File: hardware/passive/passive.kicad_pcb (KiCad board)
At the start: 2 copper layers, 45 x 17 mm, 8 parts, among them J1 i/O, J2 Conn 1, J3 Conn 2

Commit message: Passive board updates
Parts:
- H1, H2, H3, H4: footprint cycfi_library:mounting_hole_2.1mm -> cycfi_library:mounting_hole_st1.9; moved to F.Cu
- moved J3 0.50 mm to (143.3, 108.5)
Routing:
- net out-: track 21.7 -> 24.2 mm
- net int_coil+: track 18.3 -> 20.3 mm
- removed copper zone on B.Cu, net int_coil+
- removed copper zone on B.Cu, net out-
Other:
- board text added: "XR Spectra Passive v1.01"
- board text removed: "XR Spectra Passive v1.0"
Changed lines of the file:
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@@
     (thickness 1.6)
     (drawings 24)
-    (tracks 42)
+    (tracks 47)
     (zones 0)
     (modules 8)
@@
     (44 Edge.Cuts user)
     (45 Margin user)
-    (46 B.CrtYd user hide)
-    (47 F.CrtYd user hide)
-    (48 B.Fab user hide)
-    (49 F.Fab user hide)
+    (46 B.CrtYd user)
+    (47 F.CrtYd user)
+    (48 B.Fab user)
+    (49 F.Fab user)
   )
   (setup
@@
     (add_net out-)
   )
+  (module cycfi_library:mounting_hole_st1.9 (layer F.Cu)
+    (at 148 115)
+    (descr "Mounting Hole 2.1mm, no annular")
+    (tags "mounting hole 2.1mm no annular")
+    (attr virtual)
+    (fp_text reference H4 (at 0 -3.2) (layer F.SilkS) hide
+      (effects (font (size 1 1) (thickness 0.15)))
+    )
+    (fp_text value MountingHole (at 0 3.2) (layer F.Fab) hide
+      (effects (font (size 1 1) (thickness 0.15)))
+    )
+    (fp_text user %R (at 0.3 0) (layer F.Fab)
+      (effects (font (size 1 1) (thickness 0.15)))
+    )
+    (fp_circle (center 0 0) (end 1.75 0) (layer F.CrtYd) (width 0.05))
+    (pad "" np_thru_hole circle (at 0 0) (size 2 2) (drill 2) (layers *.Cu *.Mask))
+  )
+  (module cycfi_library:mounting_hole_st1.9 (layer F.Cu)
+    (at 148 102)
+    (descr "Mounting Hole 2.1mm, no annular")
+    (tags "mounting hole 2.1mm no annular")
+    (attr virtual)
+    (fp_text reference H3 (at 0 -3.2 180) (layer F.SilkS) hide
+      (effects (font (size 1 1) (thickness 0.15)))
+    )
+    (fp_text value MountingHole (at 0 3.2 180) (layer F.Fab) hide
+      (effects (font (size 1 1) (thickness 0.15)))
+    )
+    (fp_text user %R (at 0.3 0 180) (layer F.Fab)
+      (effects (font (size 1 1) (thickness 0.15)))
+    )
+    (fp_circle (center 0 0) (end 1.75 0) (layer F.CrtYd) (width 0.05))
+    (pad "" np_thru_hole circle (at 0 0) (size 2 2) (drill 2) (layers *.Cu *.Mask))
+  )
+  (module cycfi_library:mounting_hole_st1.9 (layer F.Cu)
+    (at 107 115)
+    (descr "Mounting Hole 2.1mm, no annular")
+    (tags "mounting hole 2.1mm no annular")
+    (attr virtual)
+    (fp_text reference H2 (at 0 -3.2) (layer F.SilkS) hide
+      (effects (font (size 1 1) (thickness 0.15)))
+    )
+    (fp_text value MountingHole (at 0 3.2) (layer F.Fab) hide
+      (effects (font (size 1 1) (thickness 0.15)))
+    )
+    (fp_text user %R (at 0.3 0) (layer F.Fab)
+      (effects (font (size 1 1) (thickness 0.15)))
+    )
+    (fp_circle (center 0 0) (end 1.75 0) (layer F.CrtYd) (width 0.05))
+    (pad "" np_thru_hole circle (at 0 0) (size 2 2) (drill 2) (layers *.Cu *.Mask))
+  )
+  (module cycfi_library:mounting_hole_st1.9 (layer F.Cu)
+    (at 107 102)
+    (descr "Mounting Hole 2.1mm, no annular")
+    (tags "mounting hole 2.1mm no annular")
+    (attr virtual)
+    (fp_text reference H1 (at 0 -3.2) (layer F.SilkS) hide
+      (effects (font (size 1 1) (thickness 0.15)))
+    )
+    (fp_text value MountingHole (at 0 3.2) (layer F.Fab) hide
+      (effects (font (size 1 1) (thickness 0.15)))
+    )
+    (fp_text user %R (at 0.3 0) (layer F.Fab)
+      (effects (font (size 1 1) (thickness 0.15)))
+    )
+    (fp_circle (center 0 0) (end 1.75 0) (layer F.CrtYd) (width 0.05))
+    (pad "" np_thru_hole circle (at 0 0) (size 2 2) (drill 2) (layers *.Cu *.Mask))
+  )
   (module cycfi_library:pin_socket_2x3p_1.00mm_smd_vertical (layer B.Cu)
     (at 146.5 108.5 90)
@@
   )
   (module cycfi_library:pin_socket_2x3p_1.00mm_smd_vertical (layer B.Cu)
-    (at 142.8 108.5 90)
+    (at 143.3 108.5 90)
     (descr "surface-mounted straight pin header, 2x03, 1.00mm pitch, double rows")
     (tags "Surface mounted pin header SMD 2x03 1.00mm double row")
@@
       (rotate (xyz 0 0 0))
     )
-  )
-  (module cycfi_library:mounting_hole_2.1mm (layer B.Cu)
-    (at 148 115)
-    (descr "Mounting Hole 2.1mm, no annular")
-    (tags "mounting hole 2.1mm no annular")
-    (attr virtual)
-    (fp_text reference H4 (at 0 3.2) (layer B.SilkS) hide
-      (effects (font (size 1 1) (thickness 0.15)) (justify mirror))
-    )
-    (fp_text value MountingHole (at 0 -3.2) (layer B.Fab)
-      (effects (font (size 1 1) (thickness 0.15)) (justify mirror))
-    )
-    (fp_text user %R (at 0.3 0) (layer B.Fab)
-      (effects (font (size 1 1) (thickness 0.15)) (justify mirror))
-    )
-    (fp_circle (center 0 0) (end 2.35 0) (layer B.CrtYd) (width 0.05))
-    (pad "" np_thru_hole circle (at 0 0) (size 2.1 2.1) (drill 2.1) (layers *.Cu *.Mask))
-  )
-  (module cycfi_library:mounting_hole_2.1mm (layer B.Cu)
-    (at 148 102)
-    (descr "Mounting Hole 2.1mm, no annular")
-    (tags "mounting hole 2.1mm no annular")
-    (attr virtual)
-    (fp_text reference H3 (at 0 3.2) (layer B.SilkS) hide
-      (effects (font (size 1 1) (thickness 0.15)) (justify mirror))
-    )
-    (fp_text value MountingHole (at 0 -3.2) (layer B.Fab)
-      (effects (font (size 1 1) (thickness 0.15)) (justify mirror))
-    )
-    (fp_text user %R (at 0.3 0) (layer B.Fab)
-      (effects (font (size 1 1) (thickness 0.15)) (justify mirror))
-    )
-    (fp_circle (center 0 0) (end 2.35 0) (layer B.CrtYd) (width 0.05))
-    (pad "" np_thru_hole circle (at 0 0) (size 2.1 2.1) (drill 2.1) (layers *.Cu *.Mask))
-  )
-  (module cycfi_library:mounting_hole_2.1mm (layer B.Cu)
-    (at 107 115)
-    (descr "Mounting Hole 2.1mm, no annular")
-    (tags "mounting hole 2.1mm no annular")
-    (attr virtual)
-    (fp_text reference H2 (at 0 3.2) (layer B.SilkS) hide
-      (effects (font (size 1 1) (thickness 0.15)) (justify mirror))
-    )
-    (fp_text value MountingHole (at 0 -3.2) (layer B.Fab)
-      (effects (font (size 1 1) (thickness 0.15)) (justify mirror))
-    )
-    (fp_text user %R (at 0.3 0) (layer B.Fab)
-      (effects (font (size 1 1) (thickness 0.15)) (justify mirror))
-    )
-    (fp_circle (center 0 0) (end 2.35 0) (layer B.CrtYd) (width 0.05))
-    (pad "" np_thru_hole circle (at 0 0) (size 2.1 2.1) (drill 2.1) (layers *.Cu *.Mask))
-  )
-  (module cycfi_library:mounting_hole_2.1mm (layer B.Cu)
-    (at 107 102)
-    (descr "Mounting Hole 2.1mm, no annular")
-    (tags "mounting hole 2.1mm no annular")
-    (attr virtual)
-    (fp_text reference H1 (at 0 3.2) (layer B.SilkS) hide
-      (effects (font (size 1 1) (thickness 0.15)) (justify mirror))
-    )
-    (fp_text value MountingHole (at 0 -3.2) (layer B.Fab)
-      (effects (font (size 1 1) (thickness 0.15)) (justify mirror))
-    )
-    (fp_text user %R (at 0.3 0) (layer B.Fab)
-      (effects (font (size 1 1) (thickness 0.15)) (justify mirror))
-    )
-    (fp_circle (center 0 0) (end 2.35 0) (layer B.CrtYd) (width 0.05))
-    (pad "" np_thru_hole circle (at 0 0) (size 2.1 2.1) (drill 2.1) (layers *.Cu *.Mask))
   )
   (module cycfi_library:cycfi-logo-12mm (layer F.Cu)
@@
   (gr_line (start 114 114.8) (end 111 114.8) (layer F.SilkS) (width 0.12))
   (gr_line (start 114 102.2) (end 114 114.8) (layer F.SilkS) (width 0.12))
-  (gr_text "XR Spectra Passive v1.0" (at 108.5 108.5 -90) (layer F.SilkS)
+  (gr_text "XR Spectra Passive v1.01" (at 108.5 108.5 -90) (layer F.SilkS)
     (effects (font (size 0.5 0.5) (thickness 0.125) italic))
   )
@@
   (segment (start 145.3 106.7) (end 145.5 106.9) (width 0.2) (layer B.Cu) (net 4))
   (segment (start 145.3 105.3) (end 145.3 106.7) (width 0.2) (layer B.Cu) (net 4))
+  (segment (start 145.5 106.9) (end 146.5 106.9) (width 0.25) (layer B.Cu) (net 4))
+  (segment (start 146.5 106.9) (end 147.5 106.9) (width 0.25) (layer B.Cu) (net 4))
   (segment (start 138.5 112.7) (end 138.5 113.5) (width 0.2) (layer F.Cu) (net 5))
   (segment (start 137.9 112.1) (end 138.5 112.7) (width 0.2) (layer F.Cu) (net 5))
@@
   (segment (start 140.7 111.6) (end 140.7 111.2) (width 0.2) (layer F.Cu) (net 5))
   (segment (start 140.2 112.1) (end 140.7 111.6) (width 0.2) (layer F.Cu) (net 5))
+  (segment (start 141.8 106.9) (end 142.3 106.9) (width 0.25) (layer B.Cu) (net 5))
+  (segment (start 142.3 106.9) (end 143.3 106.9) (width 0.25) (layer B.Cu) (net 5))
+  (segment (start 143.3 106.9) (end 144.3 106.9) (width 0.25) (layer B.Cu) (net 5))
   (zone (net 1) (net_name GND) (layer F.Cu) (hatch edge 0.508)
-    (connect_pads yes (clearance 0.254))
+    (connect_pads (clearance 0.254))
     (min_thickness 0.254)
     (fill yes (arc_segments 32) (thermal_gap 0.508) (thermal_bridge_width 0.508))
@@
     )
   )
-  (zone (net 4) (net_name int_coil+) (layer B.Cu) (hatch edge 0.508)
-    (connect_pads yes (clearance 0.254))
+  (zone (net 1) (net_name GND) (layer B.Cu) (hatch edge 0.508)
+    (connect_pads (clearance 0.254))
     (min_thickness 0.254)
     (fill yes (arc_segments 32) (thermal_gap 0.508) (thermal_bridge_width 0.508))
     (polygon
       (pts
-        (xy 148 108) (xy 145 108) (xy 145 105.25) (xy 148 105.25)
+        (xy 150 117) (xy 105 117) (xy 105 100) (xy 150 100)
       )
     )
-  )
-  (zone (net 1) (net_name GND) (layer B.Cu) (hatch edge 0.508)
-    (connect_pads yes (clearance 0.254))
-    (min_thickness 0.254)
-    (fill yes (arc_segments 32) (thermal_gap 0.508) (thermal_bridge_width 0.508))
-    (polygon
-      (pts
-        (xy 150 109.3) (xy 148.5 109.3) (xy 148.5 104.3) (xy 150 104.3)
-      )
-    )
-  )
-  (zone (net 1) (net_name GND) (layer B.Cu) (hatch edge 0.508)
-    (connect_pads yes (clearance 0.254))
-    (min_thickness 0.254)
-    (fill yes (arc_segments 32) (thermal_gap 0.508) (thermal_bridge_width 0.508))
-    (polygon
-      (pts
-        (xy 150 104.5) (xy 140.5 104.5) (xy 140.5 108.5) (xy 150 108.5) (xy 150 117)
-        (xy 105 117) (xy 105 100) (xy 150 100)
-      )
-    )
-  )
-  (zone (net 5) (net_name out-) (layer B.Cu) (hatch edge 0.508)
-    (connect_pads yes (clearance 0.2))
-    (min_thickness 0.2)
-    (fill yes (arc_segments 32) (thermal_gap 0.5) (thermal_bridge_width 0.5))
-    (polygon
-      (pts
-        (xy 144.5 108) (xy 141.3 108) (xy 141.3 105.25) (xy 144.5 105.25)
-      )
-    )

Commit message: updates for v1.01
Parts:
- moved J3 0.20 mm to (143.1, 108.5)

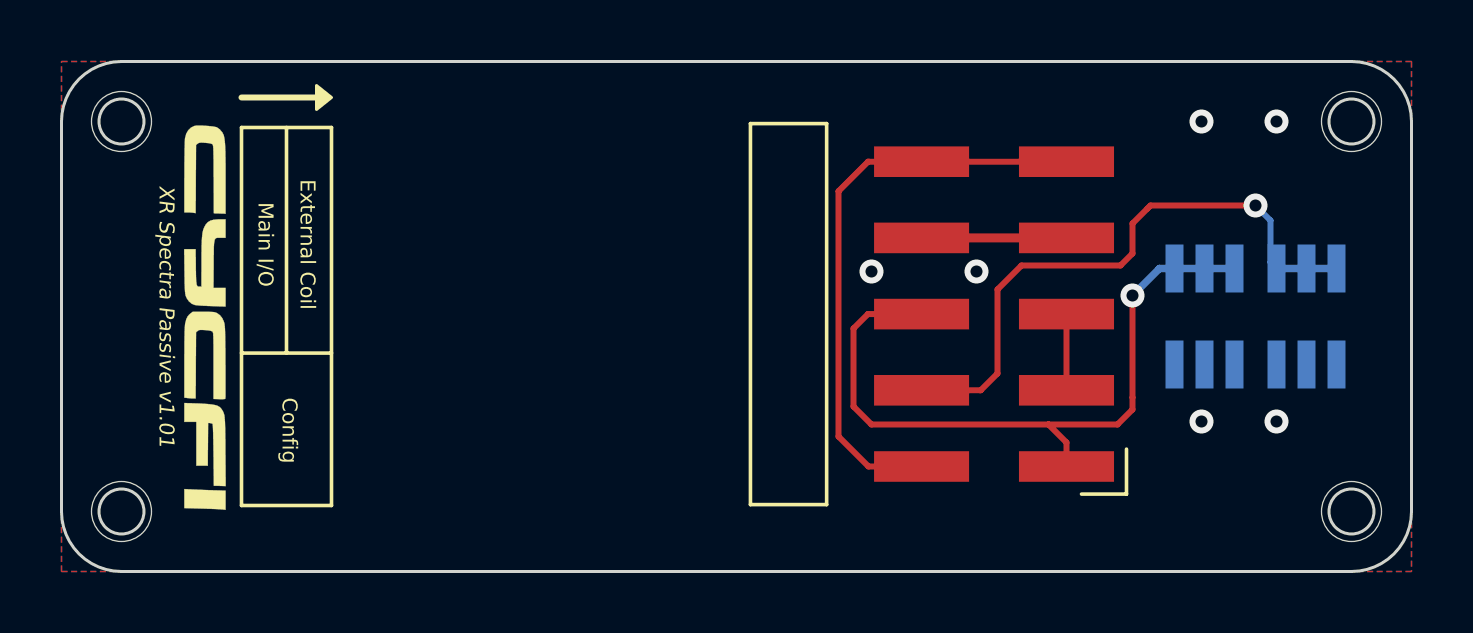
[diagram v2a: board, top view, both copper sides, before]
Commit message: Upgraded to KiCad 6
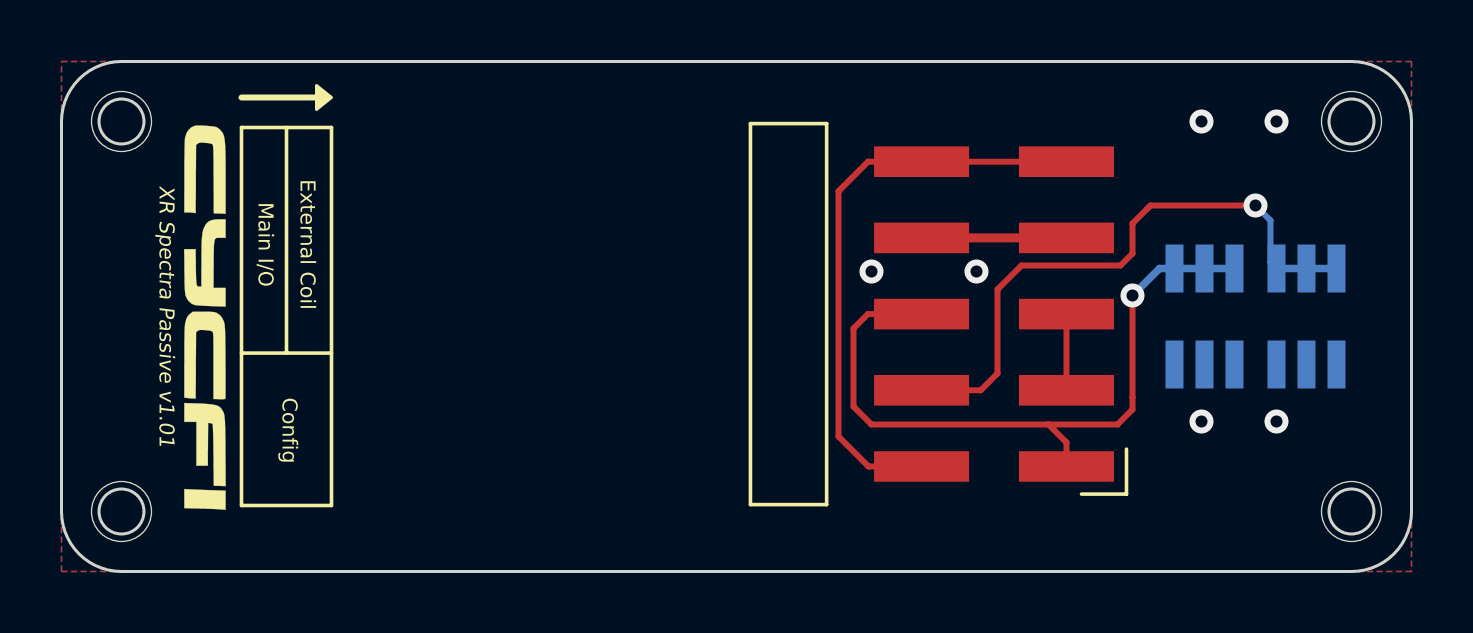
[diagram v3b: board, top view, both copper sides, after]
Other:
- net class Default removed

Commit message: v2.0 layout
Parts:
- removed J3: Conn 2, cycfi_library:pin_socket_2x3p_1.00mm_smd_vertical
- J1: value i/O -> I/O
- J2: value Conn 1 -> conn_2x2; footprint cycfi_library:pin_socket_2x3p_1.00mm_smd_vertical -> cycfi_library:pin_socket_2x2p_2.00mm_smd_vertical
- moved J2 1.00 mm to (147.5, 108.5)
- moved J1 0.40 mm to (136.1, 108.4)
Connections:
- net ext_coil+ renamed out+
- J2 pad 1: GND -> unconnected-(J2-Pad1)
- J2 pad 3: GND -> out-
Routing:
- net int_coil+: track 20.3 -> 19.1 mm
- net out-: track 24.2 -> 25.3 mm
- net GND: vias 6 -> 8
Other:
- outline, holes or cut-outs redrawn

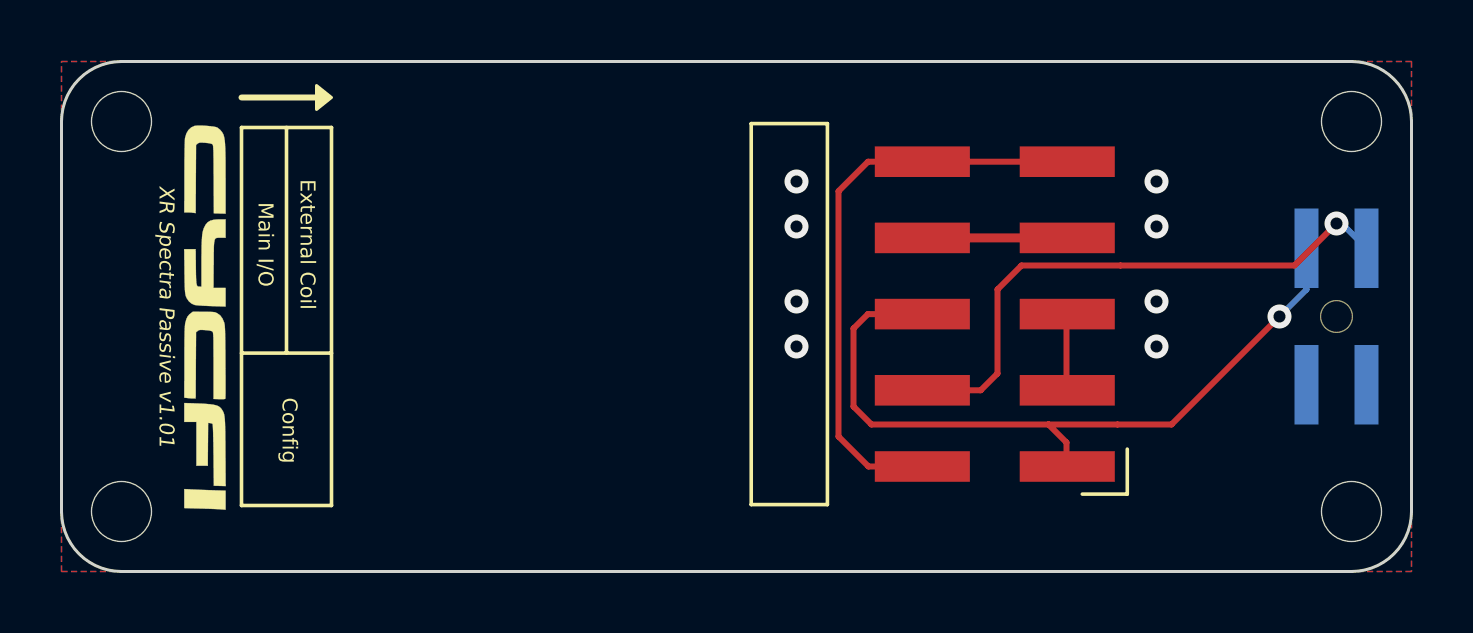
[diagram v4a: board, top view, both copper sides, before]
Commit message: Flipped top and bottom for consistency
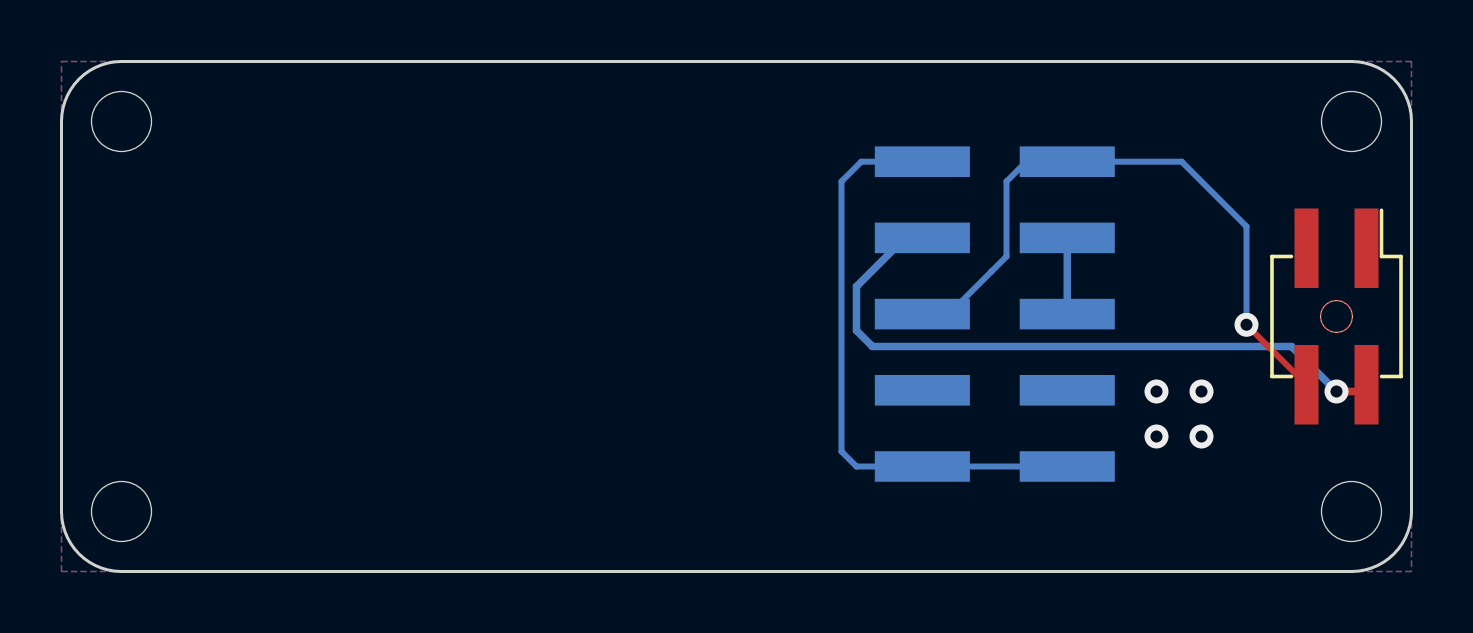
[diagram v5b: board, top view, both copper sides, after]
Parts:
- G***, J1: moved to B.Cu
- J2: moved to F.Cu
- turned J2 to -90 degrees
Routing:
- net GND: track 4.83 -> 0.00 mm, vias 8 -> 4
- net out-: track 25.3 -> 21.4 mm
- net int_coil+: track 19.1 -> 22.3 mm
